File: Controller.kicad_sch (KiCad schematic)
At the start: 14 parts, among them J8 Conn_01x05_Socket, U7 AVR32EA28, U9 MCP2515-xSO, U9 TCAN330

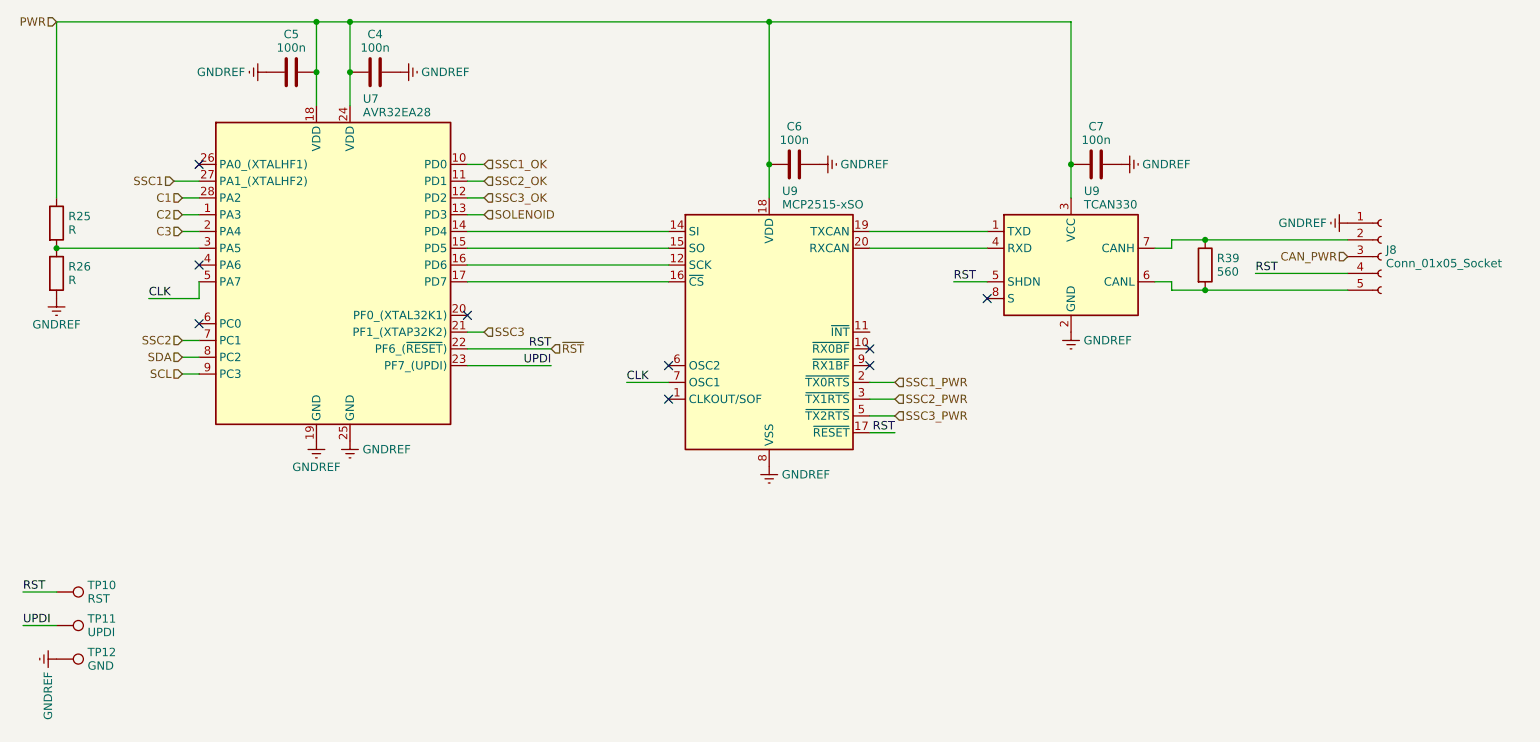
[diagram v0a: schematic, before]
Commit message: 
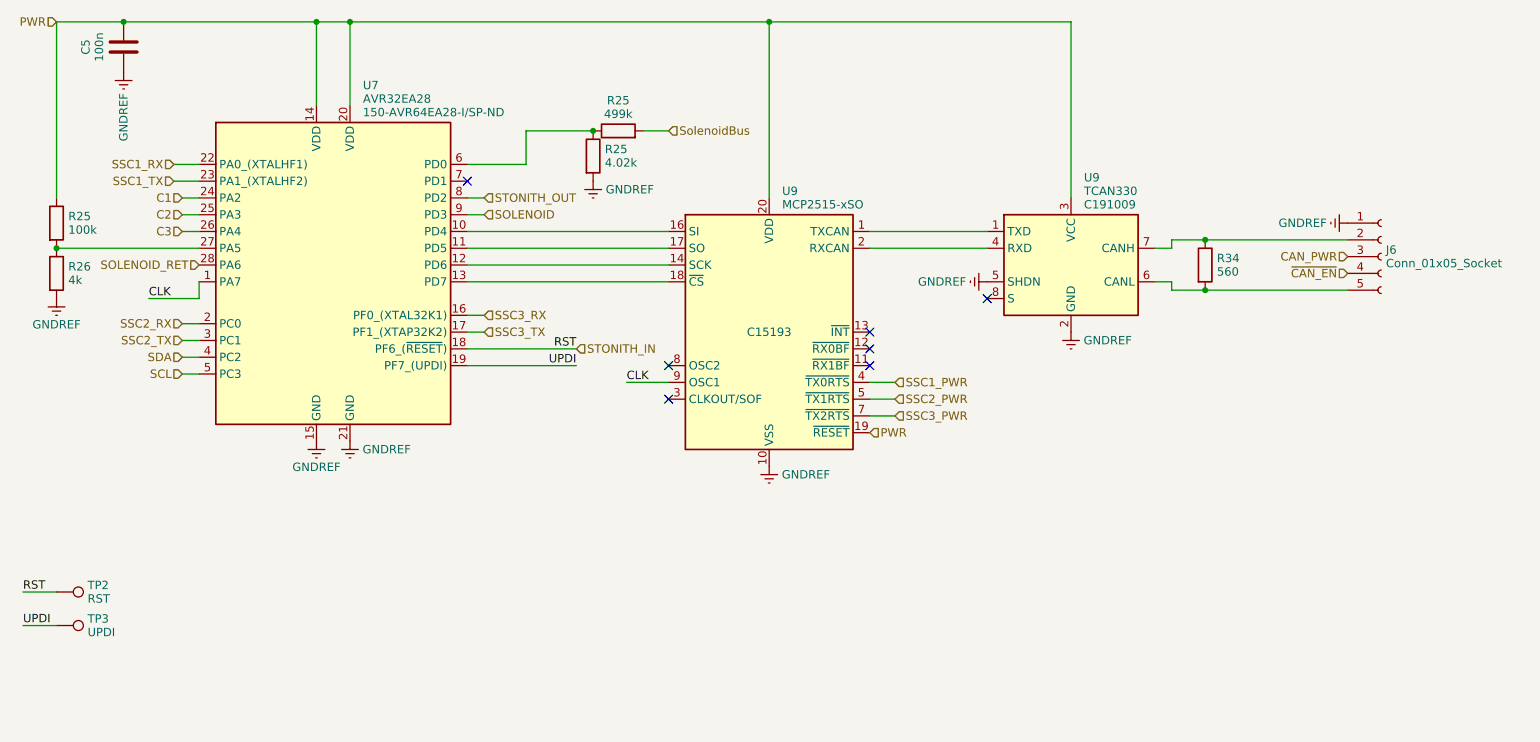
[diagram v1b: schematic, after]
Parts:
- removed C4, C6, C7: 100n, Capacitor_SMD:C_0603_1608Metric, symbol Device:C
- removed TP12: GND, TestPoint:TestPoint_Pad_D1.0mm, symbol Connector:TestPoint
- added R25: 499k, Resistor_SMD:R_0402_1005Metric, symbol Project:R
- added R25: 4.02k, Resistor_SMD:R_0402_1005Metric, symbol Project:R
- C5: MPN (none) -> C14663
- J6: renamed from J8; now left out of the parts list
- R25: value R -> 100k; footprint Resistor_SMD:R_0603_1608Metric -> Resistor_SMD:R_0402_1005Metric; symbol Device:R -> Project:R; MPN (none) -> C25741
- R26: value R -> 4k; footprint Resistor_SMD:R_0603_1608Metric -> Resistor_SMD:R_0402_1005Metric; symbol Device:R -> Project:R; MPN (none) -> C2692757
- R34: renamed from R39; footprint Resistor_SMD:R_0603_1608Metric -> Resistor_SMD:R_0402_1005Metric; symbol Device:R -> Project:R; MPN (none) -> C163460
- U7: footprint Package_DFN_QFN:VQFN-28-1EP_4x4mm_P0.45mm_EP2.4x2.4mm -> Package_SO:SSOP-28_5.3x10.2mm_P0.65mm; symbol Project:AVR32EA28 -> Project:AVR64EA28; Digikey Part # (none) -> 150-AVR64EA28-I/SP-ND
- U9: footprint Package_TO_SOT_SMD:SOT-23-8 -> Package_SO:SOIC-8_3.9x4.9mm_P1.27mm; symbol Interface_CAN_LIN:TCAN330 -> Project:TCAN330; MPN (none) -> C191009; now left out of the parts list
- U9: footprint Package_DFN_QFN:QFN-20-1EP_4x4mm_P0.5mm_EP2.7x2.7mm -> Package_SO:TSSOP-20_4.4x6.5mm_P0.65mm; JLC Part # (none) -> C15193
- renumbered TP10 to TP2, TP11 to TP3
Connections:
- net SSC1 is gone; now on an unnamed net: U7.27 (PA5)
- net SSC1_OK is gone; now on an unnamed net: U7.10 (PD4)
- net SSC3 is gone; now on net GNDREF: U7.21 (GND)
- net SSC3_OK is gone; now on an unnamed net: U7.12 (PD6)
- net C1: now also U7.24 (PA2); no longer U7.28 (PA2)
- net C2: now also U7.25 (PA3); no longer U7.1 (PA3)
- net C3: now also U7.26 (PA4); no longer U7.2 (PA4)
- net CLK: now also U7.1 (PA7), U9.9 (OSC1); no longer U7.5 (PA7), U9.7 (OSC1)
- net GNDREF: now also U7.15 (GND), U9.10 (VSS), U9.5 (SHDN), R25.2; no longer U7.19 (GND), U7.25 (GND), U9.8 (VSS)
- net PWR: now also U7.14 (VDD), U7.20 (VDD), U9.19 (~{RESET}), U9.20 (VDD); no longer U7.18 (VDD), U7.24 (VDD), U9.18 (VDD)
- net SCL: now also U7.5 (PC3); no longer U7.9 (PC3)
- net SDA: now also U7.4 (PC2); no longer U7.8 (PC2)
- net SOLENOID: now also U7.9 (PD3); no longer U7.13 (PD3)
- net SSC1_PWR: now also U9.4 (~{TX0RTS}); no longer U9.2 (~{TX0RTS})
- net SSC2_PWR: now also U9.5 (~{TX1RTS}); no longer U9.3 (~{TX1RTS})
- net SSC3_PWR: now also U9.7 (~{TX2RTS}); no longer U9.5 (~{TX2RTS})
- net UPDI: now also U7.19 (PF7_(UPDI)); no longer U7.23 (PF7_(UPDI))
- net at U9.1 (TXD): now also U9.1 (TXCAN); no longer U9.19 (TXCAN)
- net at U9.4 (RXD): now also U9.2 (RXCAN); no longer U9.20 (RXCAN)
- net at U9.12 (~{RX0BF}): no longer U7.16 (PD6)
- net at U9.14 (SCK): no longer U7.14 (PD4)
- net at U9.16 (SI): no longer U7.17 (PD7)
- net at R25.2, R26.1: no longer U7.3 (PA5)
- net at U7.6 (PD0): now also R25.1, R25.1
- net SSC2: no longer names the net of U7.7 (PD1)
- net SSC2_OK: no longer names the net of U7.11 (PD5)
- net SSC2_OK: now also U9.17 (SO)
- removed net ~{RST}: J6.4 (Pin_4), TP2.1, U7.22 (PF6_(~{RESET})), U9.17 (~{RESET}), U9.5 (SHDN)
- new net: U7.13 (PD7), U9.18 (~{CS})
- new net SOLENOID_RET: U7.28 (PA6)
- new net SSC1_RX: U7.22 (PA0_(XTALHF1))
- new net SSC1_TX: U7.23 (PA1_(XTALHF2))
- new net SSC2_RX: U7.2 (PC0)
- new net SSC2_TX: U7.3 (PC1)
- new net SSC3_RX: U7.16 (PF0_(XTAL32K1))
- new net SSC3_TX: U7.17 (PF1_(XTAP32K2))
- new net STONITH_IN: TP2.1, U7.18 (PF6_(~{RESET}))
- new net STONITH_OUT: U7.8 (PD2)
- new net SolenoidBus: R25.2
- new net ~{CAN_EN}: J6.4 (Pin_4)
- no-connect marks 9 -> 7
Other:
- moved on the sheet: C5
